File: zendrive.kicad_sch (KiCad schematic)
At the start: 41 parts, among them Q2 2N7002, Q3 2N7002, Q4 2N7002, SW1 SW_SPDT, U1 DG412xY, U2 OPA2134

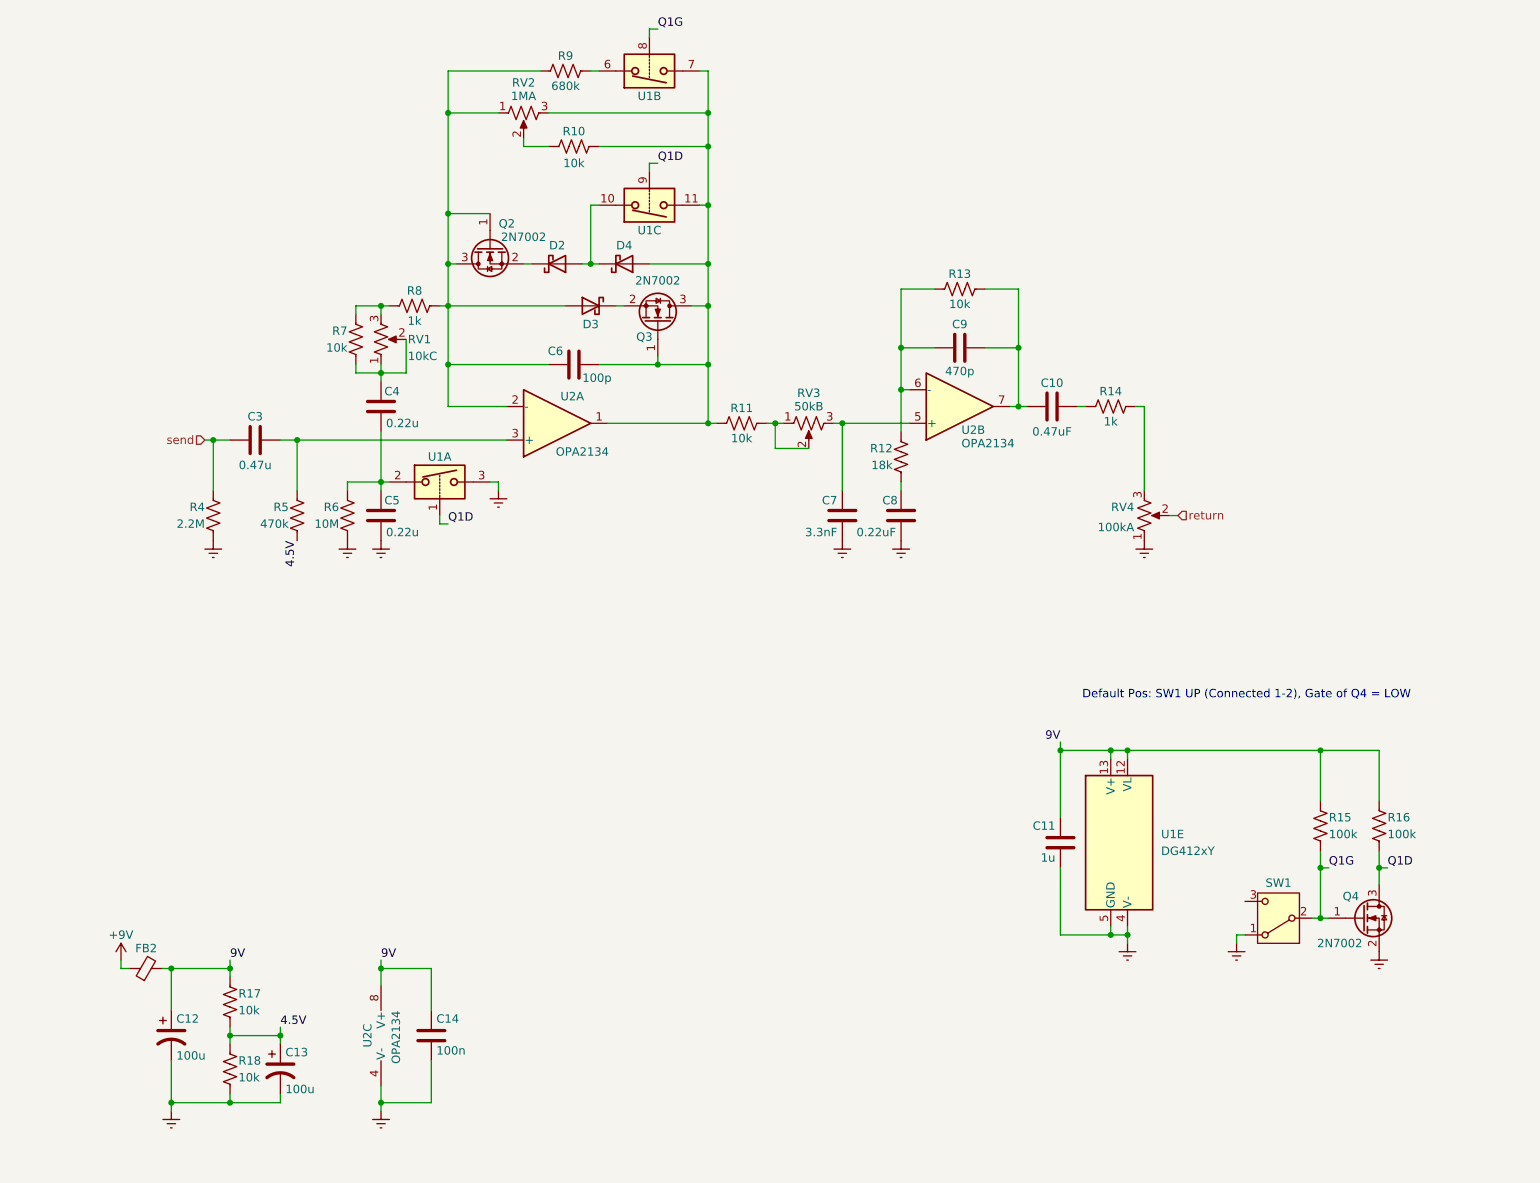
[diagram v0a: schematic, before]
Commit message: added bluesbreaker schematic
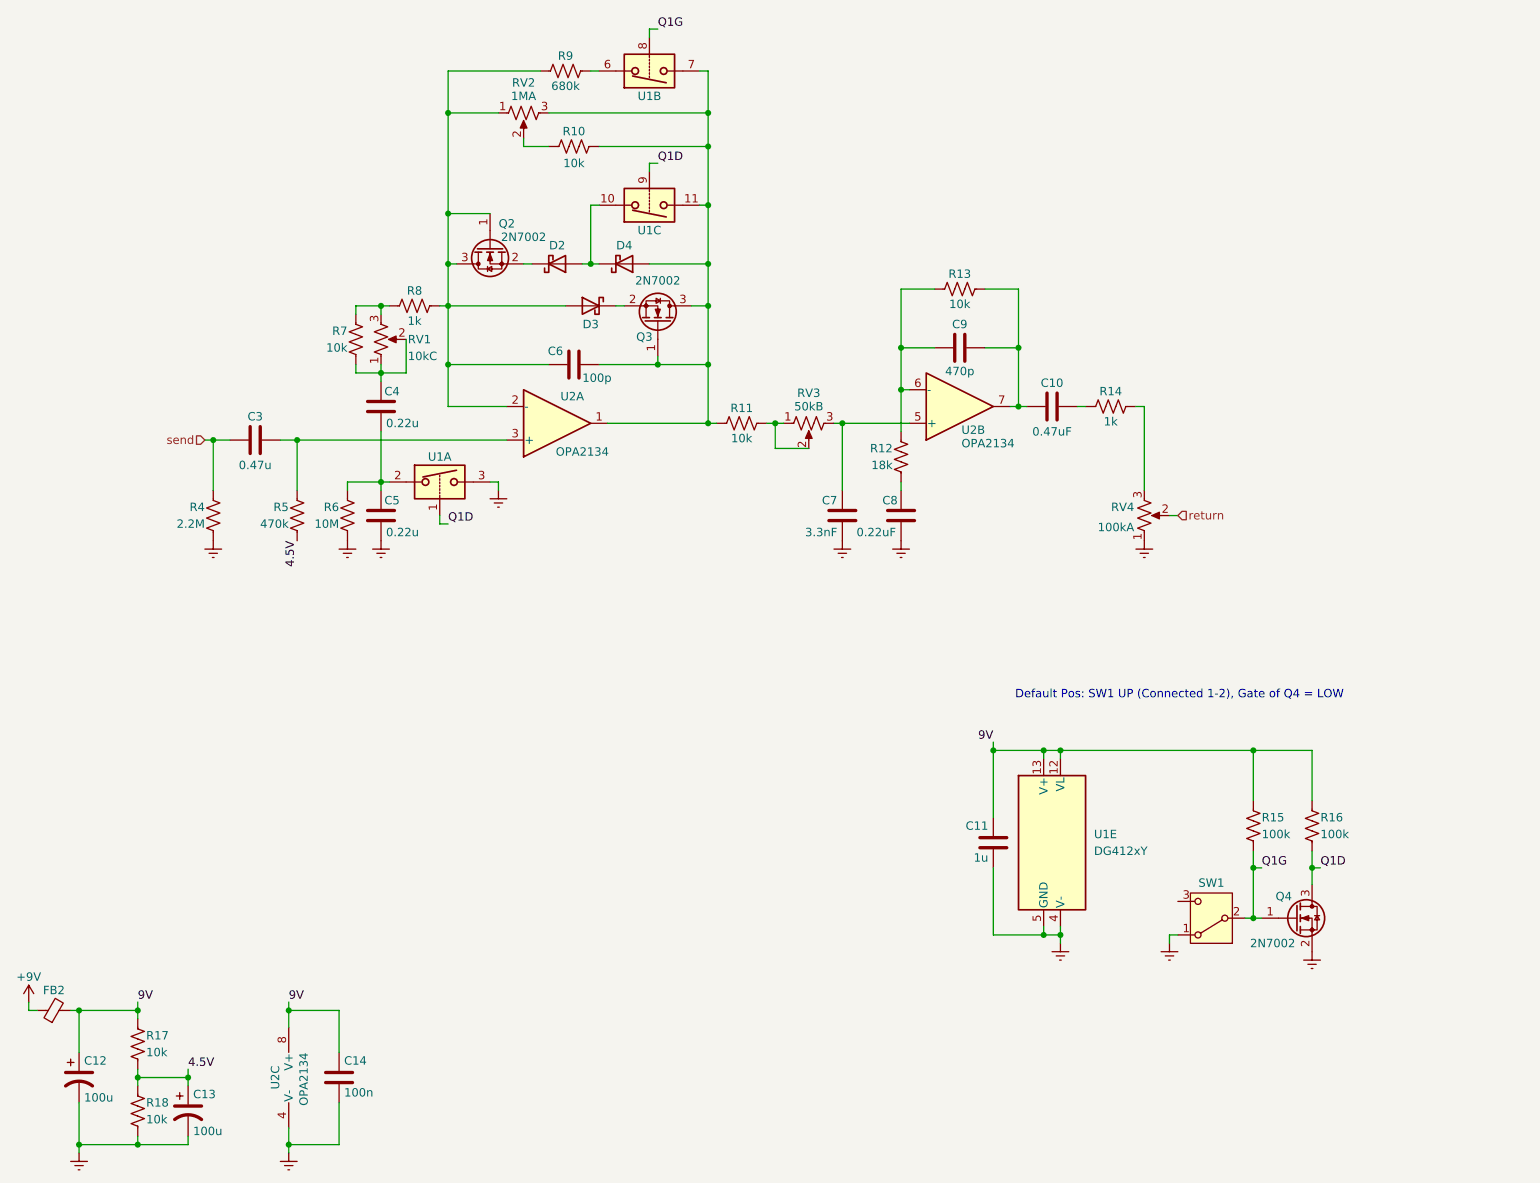
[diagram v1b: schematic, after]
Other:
- moved on the sheet: C11, C12, C13, C14, FB2, Q4, R15, R16, R17, R18, SW1, U1E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

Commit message: first route of PCB
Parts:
- C14: footprint Capacitor_SMD:C_0603_1608Metric_Pad1.08x0.95mm_HandSolder -> Capacitor_SMD:C_0805_2012Metric_Pad1.18x1.45mm_HandSolder
- C6, C9: footprint Capacitor_SMD:C_0603_1608Metric_Pad1.08x0.95mm_HandSolder -> bca-footprints:C_Ceramic_L4.0mm_W2.5mm_P2.50mm
- D2, D3, D4: footprint Diode_SMD:D_SOD-323_HandSoldering -> bca-footprints:Diode_DO-35_P5.00mm
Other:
- moved on the sheet: C11, C12, C13, C14, FB2, Q4, R15, R16, R17, R18, SW1, U1E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

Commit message: first draft PCB
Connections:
- net Earth: now also U1.11; no longer U1.3
- net Q1D: now also U1.16; no longer U1.1
- net Q1G: now also U1.1; no longer U1.8
- net at C4.1, C5.2, R6.2: now also U1.10; no longer U1.2
- net at C6.2, D4.2 (A), Q3.1 (G)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: now also U1.14, U1.3; no longer U1.11, U1.7
- net at D2.2 (A), D4.1 (K): now also U1.15; no longer U1.10
- net at R9.2: now also U1.2; no longer U1.6
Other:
- moved on the sheet: U1A, U1C, U1D

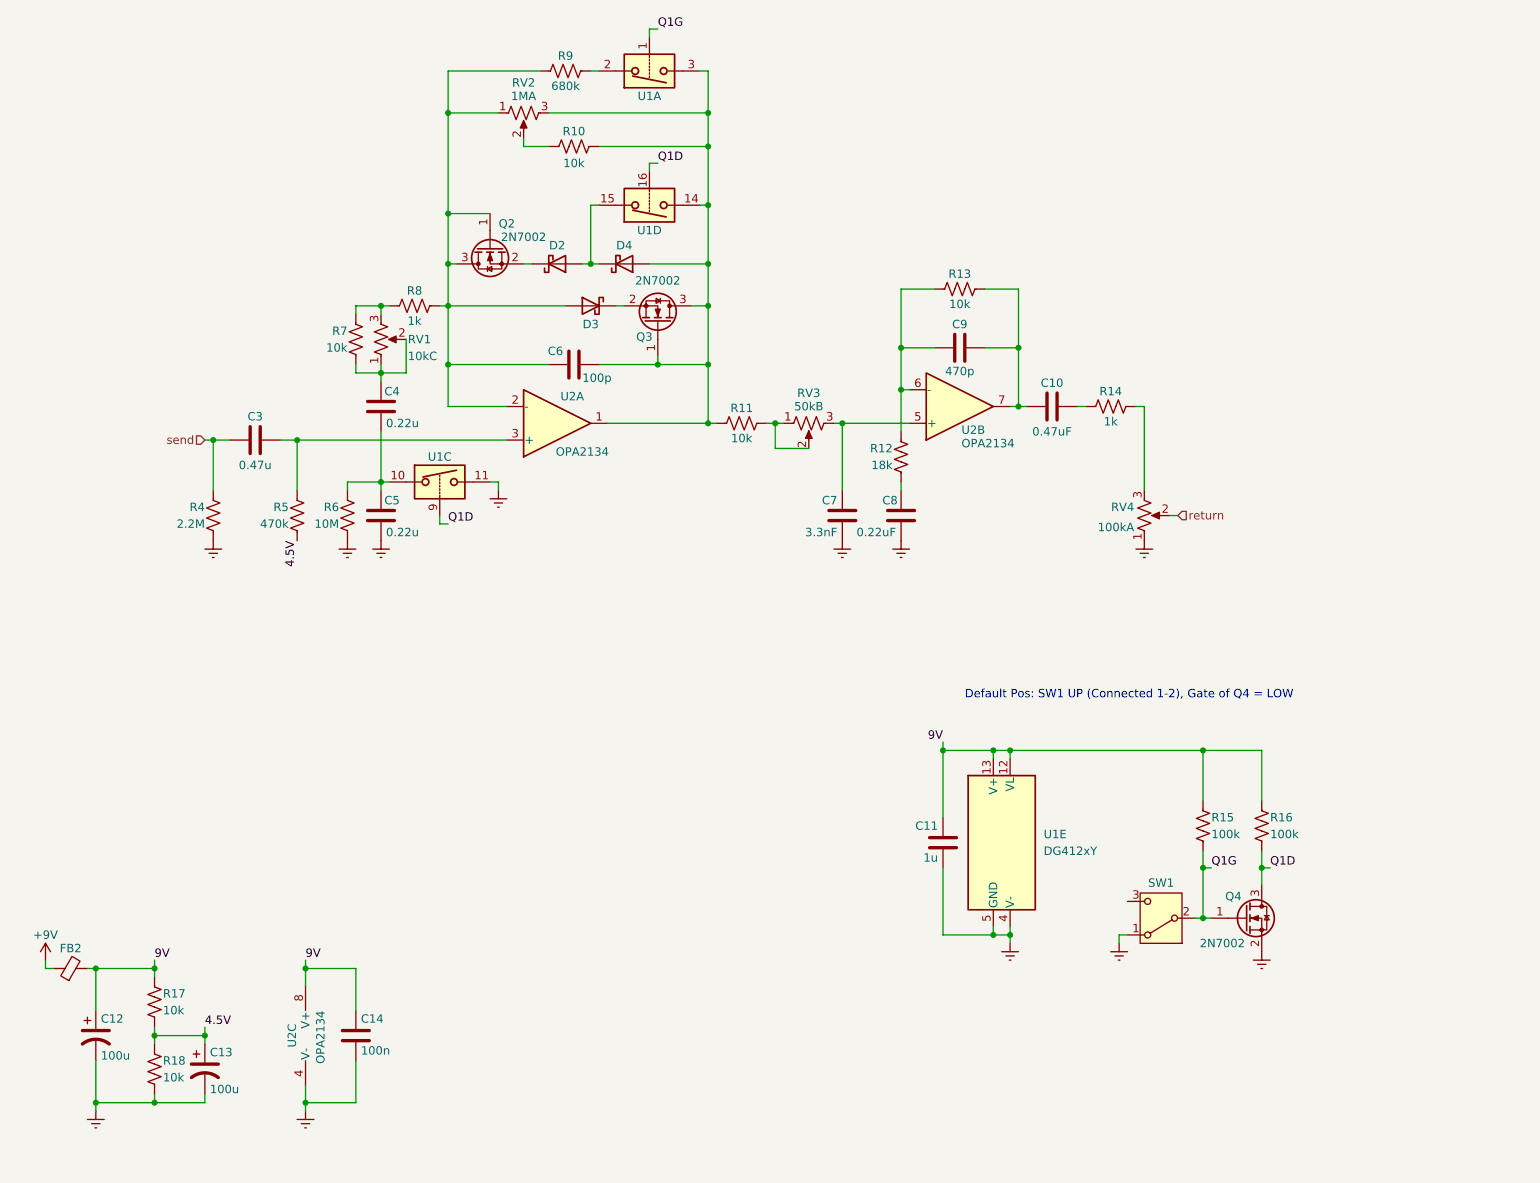
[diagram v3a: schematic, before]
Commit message: re-generated gerbers, finalized BOM
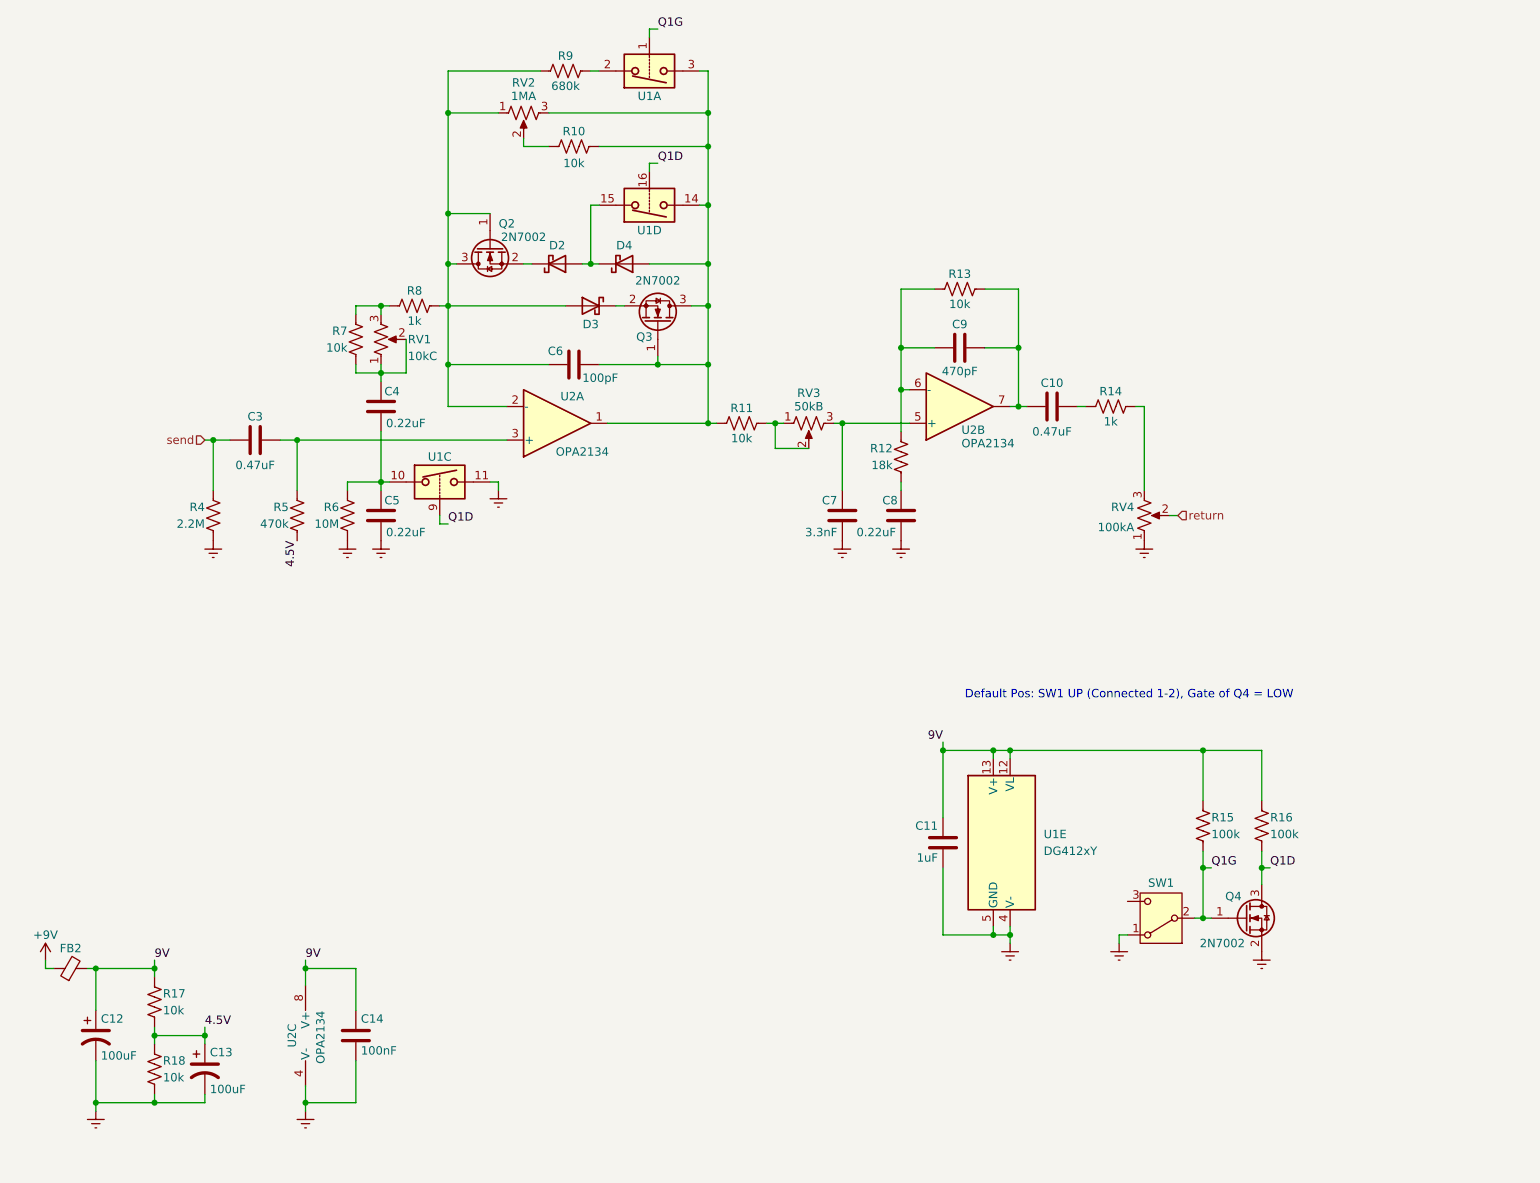
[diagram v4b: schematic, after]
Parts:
- C11: value 1u -> 1uF
- C12, C13: value 100u -> 100uF
- C14: value 100n -> 100nF
- C3: value 0.47u -> 0.47uF
- C4, C5: value 0.22u -> 0.22uF
- C6: value 100p -> 100pF
- C9: value 470p -> 470pF
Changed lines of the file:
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@@
 			)
 		)
-		(property "Value" "0.22u"
+		(property "Value" "0.22uF"
 			(at 85.852 77.47 0)
 			(effects
@@
 			)
 		)
-		(property "Value" "470p"
+		(property "Value" "470pF"
 			(at 172.72 69.596 90)
 			(effects
@@
 			)
 		)
-		(property "Value" "0.47u"
+		(property "Value" "0.47uF"
 			(at 66.04 83.82 90)
 			(effects
@@
 			)
 		)
-		(property "Value" "100u"
+		(property "Value" "100uF"
 			(at 42.672 173.228 0)
 			(effects
@@
 			)
 		)
-		(property "Value" "0.22u"
+		(property "Value" "0.22uF"
 			(at 85.852 93.98 0)
 			(effects
@@
 			)
 		)
-		(property "Value" "100p"
+		(property "Value" "100pF"
 			(at 115.57 70.612 90)
 			(effects
@@
 			)
 		)
-		(property "Value" "100n"
+		(property "Value" "100nF"
 			(at 82.042 172.466 0)
 			(effects
@@
 			)
 		)
-		(property "Value" "1u"
+		(property "Value" "1uF"
 			(at 169.418 143.256 0)
 			(effects
@@
 			)
 		)
-		(property "Value" "100u"
+		(property "Value" "100uF"
 			(at 59.182 178.308 0)
 			(effects
